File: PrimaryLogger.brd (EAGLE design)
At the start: 52.1 x 77.1 mm, 65 parts, among them J1 CONN_42.54_SCREW, J2 CONN_42.54_SCREW, J3 CONN_42.54_SCREW, J4 CONN_42.54_SCREW, J5 CONN_32.54_SCREW, Q1 DMG3404, Q2 DMG3404, U1 MIC2005, U2 MIC2091, U25 SN74AUP3G34DCU, U3 TPL5010DDC, U4 TXS0102DCU, U5 SN74LVC1G3157SC70, U6 TCS3400, U7 SHTC3DFN, U8 MCP23008QFN, U9 MCP7940SOIC

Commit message: Updated for v0.1, ready for fab
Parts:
- added C14: 0.1uF, bschulz_passives:C0603
- added JP7: JUMPER-SMT_2_NC_PASTE_SILK, SparkFun-Jumpers:SMT-JUMPER_2_NC_PASTE_SILK
- moved R10 1.02 mm to (19.7, 58.2)
- moved U3 1.02 mm to (22.7, 58.7)
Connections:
- new net N$6: C14.1, JP7.1, U3.1
- new net WAKE: U3.5, U8.14
- net 3V3: now also JP7.2; no longer U3.1
- net GND: now also C14.2
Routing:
- net WAKE: track 0.00 -> 19.6 mm, vias 0 -> 2
- net N$6: track 0.00 -> 3.26 mm
- net 3V3: track 179.7 -> 178.4 mm
- net WD_HOLD: track 4.16 -> 3.13 mm
- net GND: track 331.7 -> 332.6 mm
- net TIP: track 81.7 -> 82.6 mm
- net IO_EXP_INT: track 19.1 -> 19.7 mm
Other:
- board text added: "JP1"
- board text added: "JP2"
- board text added: "JP3"
- board text added: "JP4"
- board text added: "JP5"
- board text added: "JP6"
- board text added: "PORT1"
- board text added: "PORT2"
- board text added: "PORT3"
- board text added: "Project Hyena v0.1 Bobby Schulz UMN/GEMS"
- board text removed: "Project Hyena v0.0 Bobby Schulz UMN/GEMS"

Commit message: Updated part numbers
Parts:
- U2: value MIC2091 -> MIC2005
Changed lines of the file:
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@@
 <drawing>
 <settings>
-<setting alwaysvectorfont="no"/>
+<setting alwaysvectorfont="yes"/>
 <setting verticaltext="up"/>
 </settings>
@@
 <element name="MS1" library="bschulz" package="FEATHERWING_DIM" value="FEATHERWING_NODIM" x="50.8" y="76.2" smashed="yes" rot="R180"/>
 <element name="R1" library="bschulz_passives" package="R0603" value="100k" x="29.464" y="63.5" smashed="yes" rot="R270">
-<attribute name="DIGIKEY" value="RC0402FR-071ML" x="-32.766" y="33.02" size="1.778" layer="27" rot="R270" display="off"/>
+<attribute name="DIGIKEY" value="311-100KHRCT-ND" x="-32.766" y="33.02" size="1.778" layer="27" rot="R270" display="off"/>
 <attribute name="MF" value="Yageo" x="-32.766" y="33.02" size="1.778" layer="27" rot="R270" display="off"/>
 <attribute name="MPN" value="RC0603FR-07100KL" x="-32.766" y="33.02" size="1.778" layer="27" rot="R270" display="off"/>
@@
 </element>
 <element name="R10" library="bschulz_passives" package="R0603" value="100k" x="19.685" y="58.166" smashed="yes" rot="R270">
-<attribute name="DIGIKEY" value="RC0402FR-071ML" x="-41.275" y="8.636" size="1.778" layer="27" rot="R270" display="off"/>
+<attribute name="DIGIKEY" value="311-100KHRCT-ND" x="-41.275" y="8.636" size="1.778" layer="27" rot="R270" display="off"/>
 <attribute name="MF" value="Yageo" x="-41.275" y="8.636" size="1.778" layer="27" rot="R270" display="off"/>
 <attribute name="MPN" value="RC0603FR-07100KL" x="-41.275" y="8.636" size="1.778" layer="27" rot="R270" display="off"/>
@@
 </element>
 <element name="R2" library="bschulz_passives" package="R0603" value="100k" x="31.623" y="63.5" smashed="yes" rot="R90">
-<attribute name="DIGIKEY" value="RC0402FR-071ML" x="93.853" y="97.79" size="1.778" layer="27" rot="R90" display="off"/>
+<attribute name="DIGIKEY" value="311-100KHRCT-ND" x="93.853" y="97.79" size="1.778" layer="27" rot="R90" display="off"/>
 <attribute name="MF" value="Yageo" x="93.853" y="97.79" size="1.778" layer="27" rot="R90" display="off"/>
 <attribute name="MPN" value="RC0603FR-07100KL" x="93.853" y="97.79" size="1.778" layer="27" rot="R90" display="off"/>
@@
 </element>
 <element name="R3" library="bschulz_passives" package="R0603" value="100k" x="27.305" y="63.5" smashed="yes" rot="R270">
-<attribute name="DIGIKEY" value="RC0402FR-071ML" x="-34.925" y="25.4" size="1.778" layer="27" rot="R270" display="off"/>
+<attribute name="DIGIKEY" value="311-100KHRCT-ND" x="-34.925" y="25.4" size="1.778" layer="27" rot="R270" display="off"/>
 <attribute name="MF" value="Yageo" x="-34.925" y="25.4" size="1.778" layer="27" rot="R270" display="off"/>
 <attribute name="MPN" value="RC0603FR-07100KL" x="-34.925" y="25.4" size="1.778" layer="27" rot="R270" display="off"/>
@@
 </element>
 <element name="R4" library="bschulz_passives" package="R0603" value="100k" x="25.908" y="49.784" smashed="yes">
-<attribute name="DIGIKEY" value="RC0402FR-071ML" x="67.818" y="-12.446" size="1.778" layer="27" display="off"/>
+<attribute name="DIGIKEY" value="311-100KHRCT-ND" x="67.818" y="-12.446" size="1.778" layer="27" display="off"/>
 <attribute name="MF" value="Yageo" x="67.818" y="-12.446" size="1.778" layer="27" display="off"/>
 <attribute name="MPN" value="RC0603FR-07100KL" x="67.818" y="-12.446" size="1.778" layer="27" display="off"/>
@@
 </element>
 <element name="R41" library="bschulz_passives" package="R0603" value="100k" x="38.354" y="72.39" smashed="yes" rot="R180">
-<attribute name="DIGIKEY" value="RC0402FR-071ML" x="-14.986" y="133.35" size="1.778" layer="27" rot="R180" display="off"/>
+<attribute name="DIGIKEY" value="311-100KHRCT-ND" x="-14.986" y="133.35" size="1.778" layer="27" rot="R180" display="off"/>
 <attribute name="MF" value="Yageo" x="-14.986" y="133.35" size="1.778" layer="27" rot="R180" display="off"/>
 <attribute name="MPN" value="RC0603FR-07100KL" x="-14.986" y="133.35" size="1.778" layer="27" rot="R180" display="off"/>
@@
 </element>
 <element name="SD1" library="bschulz" package="CUSTOM-PARTS_SD_MICRO" value="MICRO_SD" x="50.038" y="70.612" smashed="yes" rot="R90">
-<attribute name="DIGIKEY" value="" x="79.248" y="84.582" size="1.778" layer="27" rot="R90" display="off"/>
-<attribute name="MF" value="" x="79.248" y="84.582" size="1.778" layer="27" rot="R90" display="off"/>
-<attribute name="MPN" value="" x="79.248" y="84.582" size="1.778" layer="27" rot="R90" display="off"/>
+<attribute name="DIGIKEY" value="114-00841-68-1-ND" x="50.038" y="70.612" size="1.778" layer="27" rot="R90" display="off"/>
+<attribute name="MF" value="Amphenol" x="50.038" y="70.612" size="1.778" layer="27" rot="R90" display="off"/>
+<attribute name="MPN" value="114-00841-68" x="50.038" y="70.612" size="1.778" layer="27" rot="R90" display="off"/>
 <attribute name="NAME" x="44.958" y="57.912" size="0.6096" layer="25" font="vector" ratio="15" rot="R180" align="center"/>
 </element>
@@
 <attribute name="VALUE" x="32.004" y="63.373" size="0.6096" layer="27" font="vector" ratio="15" rot="R270" align="center"/>
 </element>
-<element name="U2" library="bschulz" package="SOT23-5" value="MIC2091" x="25.4" y="46.99" smashed="yes" rot="R90">
-<attribute name="DIGIKEY" value="576-3891-1-ND" x="80.01" y="87.63" size="1.778" layer="27" rot="R90" display="off"/>
-<attribute name="DISP" value="MIC2091" x="80.01" y="87.63" size="1.778" layer="27" rot="R90" display="off"/>
+<element name="U2" library="bschulz" package="SOT23-5" value="MIC2005" x="25.4" y="46.99" smashed="yes" rot="R90">
+<attribute name="DIGIKEY" value="576-3462-1-ND" x="80.01" y="87.63" size="1.778" layer="27" rot="R90" display="off"/>
+<attribute name="DISP" value="MIC2005" x="80.01" y="87.63" size="1.778" layer="27" rot="R90" display="off"/>
 <attribute name="MF" value="Microchip" x="80.01" y="87.63" size="1.778" layer="27" rot="R90" display="off"/>
-<attribute name="MPN" value="MIC2091-1YM5-TR" x="80.01" y="87.63" size="1.778" layer="27" rot="R90" display="off"/>
+<attribute name="MPN" value="MIC2005A-1YM5-TR" x="80.01" y="87.63" size="1.778" layer="27" rot="R90" display="off"/>
 <attribute name="NAME" x="23.876" y="46.99" size="0.6096" layer="25" font="vector" ratio="15" rot="R180" align="center"/>
 <attribute name="VALUE" x="25.273" y="49.276" size="0.6096" layer="27" font="vector" ratio="15" rot="R180" align="center"/>
@@
 </element>
 <element name="R6" library="bschulz_passives" package="R0603" value="100k" x="10.16" y="59.69" smashed="yes" rot="R270">
-<attribute name="DIGIKEY" value="RC0402FR-071ML" x="10.16" y="59.69" size="1.778" layer="27" rot="R270" display="off"/>
+<attribute name="DIGIKEY" value="311-100KHRCT-ND" x="10.16" y="59.69" size="1.778" layer="27" rot="R270" display="off"/>
 <attribute name="MF" value="Yageo" x="10.16" y="59.69" size="1.778" layer="27" rot="R270" display="off"/>
 <attribute name="MPN" value="RC0603FR-07100KL" x="10.16" y="59.69" size="1.778" layer="27" rot="R270" display="off"/>
@@
 </element>
 <element name="R7" library="bschulz_passives" package="R0603" value="100k" x="5.08" y="59.69" smashed="yes" rot="R270">
-<attribute name="DIGIKEY" value="RC0402FR-071ML" x="5.08" y="59.69" size="1.778" layer="27" rot="R270" display="off"/>
+<attribute name="DIGIKEY" value="311-100KHRCT-ND" x="5.08" y="59.69" size="1.778" layer="27" rot="R270" display="off"/>
 <attribute name="MF" value="Yageo" x="5.08" y="59.69" size="1.778" layer="27" rot="R270" display="off"/>
 <attribute name="MPN" value="RC0603FR-07100KL" x="5.08" y="59.69" size="1.778" layer="27" rot="R270" display="off"/>
@@
 </element>
 <element name="R8" library="bschulz_passives" package="R0603" value="100k" x="20.701" y="9.525" smashed="yes" rot="R180">
-<attribute name="DIGIKEY" value="RC0402FR-071ML" x="20.701" y="9.525" size="1.778" layer="27" rot="R180" display="off"/>
+<attribute name="DIGIKEY" value="311-100KHRCT-ND" x="20.701" y="9.525" size="1.778" layer="27" rot="R180" display="off"/>
 <attribute name="MF" value="Yageo" x="20.701" y="9.525" size="1.778" layer="27" rot="R180" display="off"/>
 <attribute name="MPN" value="RC0603FR-07100KL" x="20.701" y="9.525" size="1.778" layer="27" rot="R180" display="off"/>
@@
 </element>
 <element name="R5" library="bschulz_passives" package="R0603" value="100k" x="5.715" y="49.53" smashed="yes">
-<attribute name="DIGIKEY" value="RC0402FR-071ML" x="5.715" y="49.53" size="1.778" layer="27" display="off"/>
+<attribute name="DIGIKEY" value="311-100KHRCT-ND" x="5.715" y="49.53" size="1.778" layer="27" display="off"/>
 <attribute name="MF" value="Yageo" x="5.715" y="49.53" size="1.778" layer="27" display="off"/>
 <attribute name="MPN" value="RC0603FR-07100KL" x="5.715" y="49.53" size="1.778" layer="27" display="off"/>

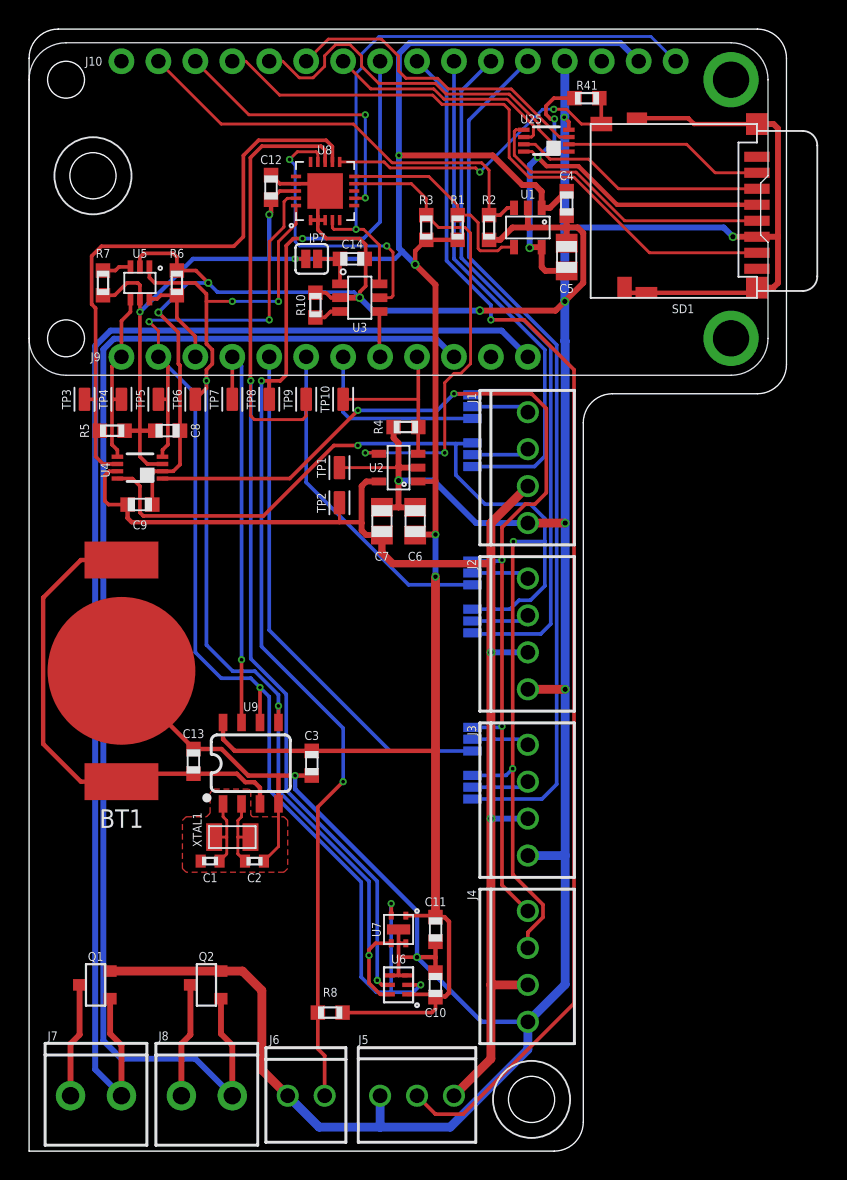
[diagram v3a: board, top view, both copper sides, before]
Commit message: Updated parts for BoM, moved designators, changed R41
Updated part numbers to generate BoM, moved `R11` designator and changed `R41` to be `R12` to match ordering of rest of board (was carry over from Resnik I think)
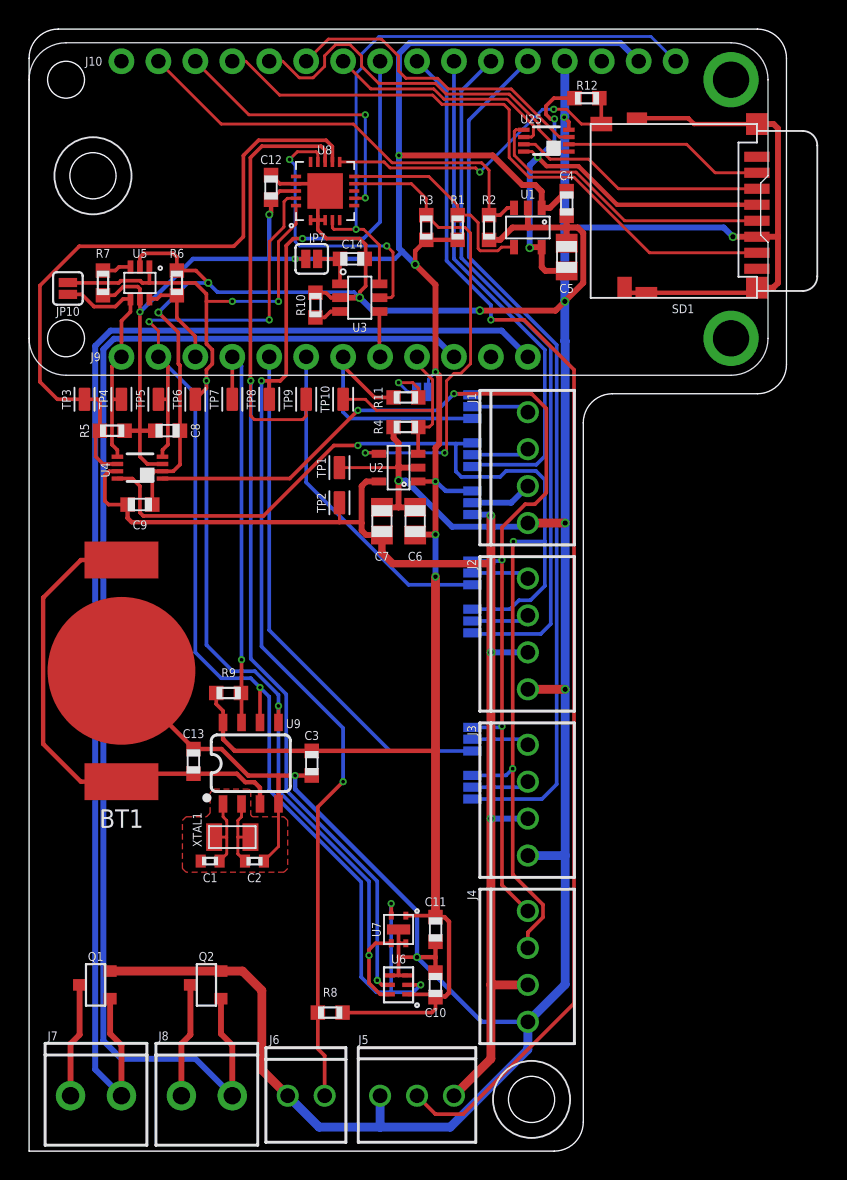
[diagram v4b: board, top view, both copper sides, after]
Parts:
- added JP10: JUMPER-SMT_2_NO_SILK, SparkFun-Jumpers:SMT-JUMPER_2_NO_SILK
- added JP8: JUMPER-SMT_3_1-NC_PASTE_SILK, SparkFun-Jumpers:SMT-JUMPER_3_1-NC_PASTE_SILK
- added JP9: JUMPER-SMT_2_NC_PASTE_SILK, SparkFun-Jumpers:SMT-JUMPER_2_NC_PASTE_SILK
- added R11, R9: 100k, bschulz_passives:R0603
- renumbered R41 to R12
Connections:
- new net N$5: JP9.1, R11.2
- new net PWR_P1: J1.3, JP8.2
- net 3V3: now also JP8.1, JP9.2, R9.2
- net 3V3_EXT: now also JP8.3; no longer J1.3
- net GPIO1D: now also R11.1
- net RTC_INT: now also R9.1
- net SDA: now also JP10.2
- net SDA_OB: now also JP10.1
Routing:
- net 3V3: track 178.4 -> 184.9 mm, vias 7 -> 9
- net SDA_OB: track 76.9 -> 82.9 mm
- net GPIO1D: track 12.9 -> 17.9 mm
- net SDA: track 12.2 -> 17.1 mm
- net I2C_EXT_EN: track 41.0 -> 45.8 mm
- net PWR_P1: track 0.00 -> 4.28 mm
- net N$5: track 0.00 -> 3.66 mm, vias 0 -> 1
- net 3V3_EXT_EN: track 12.1 -> 14.7 mm
- net 3V3_EXT: track 89.4 -> 87.7 mm, vias 2 -> 3
- net SDA_EXT: track 82.8 -> 84.5 mm
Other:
- board text added: "Core"
- board text added: "Ext"
- board text added: "GPIO"
- board text added: "Project Hyena v0.2 Bobby Schulz UMN/GEMS"
- board text removed: "JP1"
- board text removed: "JP2"
- board text removed: "JP3"
- board text removed: "JP4"
- board text removed: "JP5"
- board text removed: "JP6"
- board text removed: "Project Hyena v0.1 Bobby Schulz UMN/GEMS"

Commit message: Gerber and part updates
Added Gerber files for Advanced Circuits order, minor changes to part numbers and BoMs
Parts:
- JP1, JP2, JP3, JP4, JP5, JP6, JP8: device SparkFun-Jumpers:SMT-JUMPER_3_1-NC_PASTE_SILK -> bschulz:SMT-JUMPER_3_1-NC_PASTE_SILK
- JP10: device SparkFun-Jumpers:SMT-JUMPER_2_NO_SILK -> bschulz:SMT-JUMPER_2_NO_SILK
- JP7, JP9: device SparkFun-Jumpers:SMT-JUMPER_2_NC_PASTE_SILK -> bschulz:SMT-JUMPER_2_NC_PASTE_SILK
- R8: value 100k -> 10k
